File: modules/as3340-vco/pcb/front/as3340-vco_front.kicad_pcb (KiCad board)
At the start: 2 copper layers, 37.8 x 107.3 mm, 42 parts, among them J1 CV1, J2 CV2, J3 LINEAR, J4 TRIANGLE, J5 SAWTOOTH, J6 PULSE, J7 Conn_01x09, U1 TL074

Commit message: modules: as3340-vco: fix references
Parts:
- J1: value CV1 -> Thonkiconn SM
- J2: value CV2 -> Thonkiconn SM
- J3: value LINEAR -> Thonkiconn SM
- J4: value TRIANGLE -> Thonkiconn SM
- J5: value SAWTOOTH -> Thonkiconn SM
- J6: value PULSE -> Thonkiconn SM
- J7: value Conn_01x09 -> Pin Header 1x9
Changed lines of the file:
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@@
   (page A4)
   (title_block
-    (title "as3340-vco front board")
+    (title "as3340-vco front")
     (date 2021-12-14)
     (rev 1.0)
@@
     (46 B.CrtYd user)
     (47 F.CrtYd user)
-    (48 B.Fab user)
+    (48 B.Fab user hide)
     (49 F.Fab user hide)
   )
@@
       (effects (font (size 1 1) (thickness 0.15)) (justify mirror))
     )
-    (fp_text value Conn_01x09 (at 0 -22.65) (layer B.Fab)
+    (fp_text value "Pin Header 1x9" (at 0 -22.65) (layer B.Fab)
       (effects (font (size 1 1) (thickness 0.15)) (justify mirror))
     )
@@
       (effects (font (size 1 1) (thickness 0.15)))
     )
-    (fp_text value SAWTOOTH (at 0 -5) (layer F.Fab)
+    (fp_text value "Thonkiconn SM" (at 0 -5) (layer F.Fab)
       (effects (font (size 1 1) (thickness 0.15)))
     )
@@
       (effects (font (size 1 1) (thickness 0.15)))
     )
-    (fp_text value PULSE (at 0 -5) (layer F.Fab)
+    (fp_text value "Thonkiconn SM" (at 0 -5) (layer F.Fab)
       (effects (font (size 1 1) (thickness 0.15)))
     )
@@
       (effects (font (size 1 1) (thickness 0.15)))
     )
-    (fp_text value LINEAR (at 0 -5) (layer F.Fab)
+    (fp_text value "Thonkiconn SM" (at 0 -5) (layer F.Fab)
       (effects (font (size 1 1) (thickness 0.15)))
     )
@@
       (effects (font (size 1 1) (thickness 0.15)))
     )
-    (fp_text value TRIANGLE (at 0 -5) (layer F.Fab)
+    (fp_text value "Thonkiconn SM" (at 0 -5) (layer F.Fab)
       (effects (font (size 1 1) (thickness 0.15)))
     )
@@
       (effects (font (size 1 1) (thickness 0.15)))
     )
-    (fp_text value CV2 (at 0 -5) (layer F.Fab)
+    (fp_text value "Thonkiconn SM" (at 0 -5) (layer F.Fab)
       (effects (font (size 1 1) (thickness 0.15)))
     )
@@
       (effects (font (size 1 1) (thickness 0.15)))
     )
-    (fp_text value CV1 (at 0 -5) (layer F.Fab)
-      (effects (font (size 1 1) (thickness 0.15)))
-    )
+    (fp_text value "Thonkiconn SM" (at 0 -5) (layer F.Fab)
+      (effects (font (size 1 1) (thickness 0.15)))
+    )

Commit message: modules: as3340-vco: front: upgrade to kicad 6
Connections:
- J1 pad TN: (no net) -> unconnected-(J1-PadTN)
- J2 pad TN: (no net) -> unconnected-(J2-PadTN)
- J3 pad TN: (no net) -> unconnected-(J3-PadTN)
- J4 pad TN: (no net) -> unconnected-(J4-PadTN)
- J5 pad TN: (no net) -> unconnected-(J5-PadTN)
- J6 pad TN: (no net) -> unconnected-(J6-PadTN)
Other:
- net class Default removed

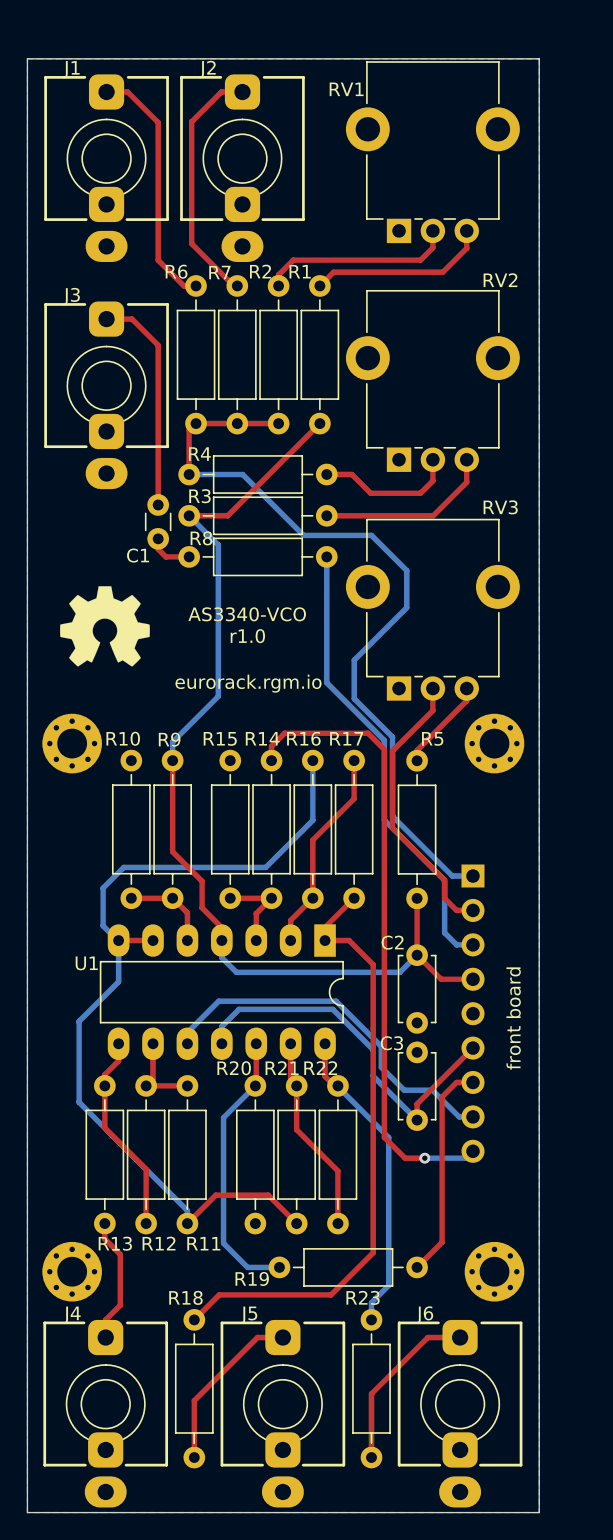
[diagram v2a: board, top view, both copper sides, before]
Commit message: modules: as3340-vco: front: revision A (redesign)
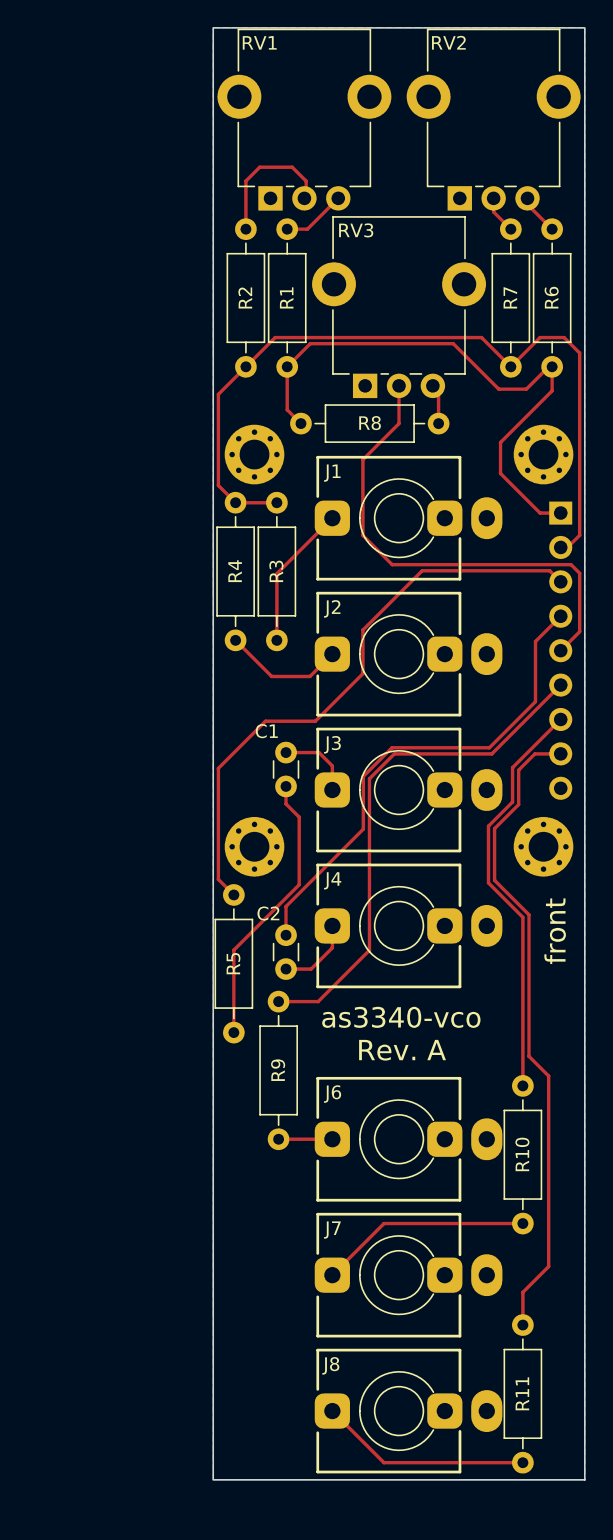
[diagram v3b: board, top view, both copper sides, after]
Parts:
- removed C3: 100n, Capacitor_THT:C_Disc_D4.7mm_W2.5mm_P5.00mm
- removed R12, R17, R22: 150k, Resistor_THT:R_Axial_DIN0207_L6.3mm_D2.5mm_P10.16mm_Horizontal
- removed R13, R18, R23: 1k, Resistor_THT:R_Axial_DIN0207_L6.3mm_D2.5mm_P10.16mm_Horizontal
- removed R14, R15, R16, R21: 100k, Resistor_THT:R_Axial_DIN0207_L6.3mm_D2.5mm_P10.16mm_Horizontal
- removed R19: 120k, Resistor_THT:R_Axial_DIN0207_L6.3mm_D2.5mm_P10.16mm_Horizontal
- removed R20: 68k, Resistor_THT:R_Axial_DIN0207_L6.3mm_D2.5mm_P10.16mm_Horizontal
- removed U1: TL074, Package_DIP:DIP-14_W7.62mm_LongPads
- added J8: Thonkiconn SM, eurorack:Jack_3.5mm_QingPu_WQP-PJ398SM_Vertical, F.Cu at (153.3, 145.2)
- added REF**: Eurorack_PCB_6HP, eurorack:Eurorack_PCB_6HP, F.Cu at (153.3, 96.6)
- C2: value 100n -> 1n; footprint Capacitor_THT:C_Disc_D4.7mm_W2.5mm_P5.00mm -> Capacitor_THT:C_Disc_D3.0mm_W1.6mm_P2.50mm
- H1, H2, H3, H4: value MountingHole -> MountingHole_Pad
- J5: value Thonkiconn SM -> Pin Header 1x9; footprint eurorack:Jack_3.5mm_QingPu_WQP-PJ398SM_Vertical -> Connector_PinHeader_2.54mm:PinHeader_1x09_P2.54mm_Vertical; moved to B.Cu
- J7: value Pin Header 1x9 -> Thonkiconn SM; footprint Connector_PinHeader_2.54mm:PinHeader_1x09_P2.54mm_Vertical -> eurorack:Jack_3.5mm_QingPu_WQP-PJ398SM_Vertical; moved to F.Cu
- R10: value 18k -> 1k
- R11: value 100k -> 1k
- R3: value 120k -> 100k
- R4: value 1.5M -> 100k
- R5: value 100k -> 1M
- R6: value 100k -> 120k
- R7: value 100k -> 1.5M
- R8: value 1M -> 100k
- R9: value 47k -> 1k
- REF**: moved to B.Cu
- moved H2 69.6 mm to (164.0, 74.5), turned to 0 degrees
- moved J5 68.9 mm to (165.2, 78.9), turned to 180 degrees
- moved J4 41.4 mm to (153.3, 109.3), turned to 90 degrees
- moved J2 38.4 mm to (153.3, 89.3), turned to 90 degrees
- moved R10 37.6 mm to (162.4, 131.3)
- moved R11 37.2 mm to (162.4, 149.0), turned to 90 degrees
- moved J3 36.8 mm to (153.3, 99.3), turned to 90 degrees
- moved H3 36.0 mm to (142.6, 103.5), turned to 0 degrees
- moved J1 34.2 mm to (153.3, 79.2), turned to 90 degrees
- moved J7 30.0 mm to (153.3, 135.1), turned to 90 degrees
- moved R9 29.0 mm to (144.4, 125.1), turned to 90 degrees
- moved R6 26.6 mm to (164.6, 68.1)
- moved H1 25.2 mm to (142.6, 74.5), turned to 0 degrees
- moved RV3 22.5 mm to (150.8, 69.5)
- moved REF** 21.8 mm to (153.2, 84.2), turned to 180 degrees
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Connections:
- C2 pad 1: +12V -> VHSI
- C2 pad 2: GND -> Net-(C2-Pad2)
- H1 pad 1: (no net) -> GND
- H2 pad 1: (no net) -> GND
- H3 pad 1: (no net) -> GND
- H4 pad 1: (no net) -> GND
- J4 pad T: Net-(J4-PadT) -> Net-(C2-Pad2)
- R10 pad 1: Net-(R10-Pad1) -> Net-(J7-PadT)
- R10 pad 2: GND -> OUT_SAWTOOTH
- R11 pad 2: VREF -> OUT_PULSE
- R3 pad 1: +12V -> VFCI
- R3 pad 2: Net-(R3-Pad2) -> Net-(J1-PadT)
- R4 pad 2: Net-(R4-Pad2) -> Net-(J2-PadT)
- R5 pad 1: +12V -> VLFI
- R5 pad 2: Net-(R5-Pad2) -> Net-(C1-Pad1)
- R6 pad 1: VFCI -> +12V
- R6 pad 2: Net-(J1-PadT) -> Net-(R6-Pad2)
- R7 pad 2: Net-(J2-PadT) -> Net-(R7-Pad2)
- R8 pad 1: VLFI -> +12V
- R8 pad 2: Net-(C1-Pad1) -> Net-(R8-Pad2)
- R9 pad 1: +12V -> Net-(J6-PadT)
- R9 pad 2: Net-(R10-Pad1) -> OUT_TRIANGLE
- RV2 pad 2: Net-(R4-Pad2) -> Net-(R7-Pad2)
- RV2 pad 3: Net-(R3-Pad2) -> Net-(R6-Pad2)
- RV3 pad 3: Net-(R5-Pad2) -> Net-(R8-Pad2)
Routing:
- net VREF: track 64.1 -> 0.00 mm
- net OUT_PULSE: track 0.00 -> 47.7 mm
- net VSO: track 46.3 -> 0.00 mm, vias 1 -> 0
- net Net-(R17-Pad1): track 44.8 -> 0.00 mm
- net OUT_TRIANGLE: track 0.00 -> 37.9 mm
- net VHSI: track 0.00 -> 36.2 mm
- net +12V: track 73.3 -> 42.1 mm
- net OUT_SAWTOOTH: track 0.00 -> 30.3 mm
- net -12V: track 27.8 -> 0.00 mm
- net VTO: track 27.3 -> 0.00 mm
- net Net-(R22-Pad1): track 23.0 -> 0.00 mm
- net Net-(R19-Pad2): track 20.6 -> 0.00 mm
- net Net-(C1-Pad1): track 3.28 -> 20.6 mm
- net VP: track 16.1 -> 0.00 mm
- net Net-(J7-PadT): track 0.00 -> 15.6 mm
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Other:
- board size 37.8 x 107.3 mm -> 27.4 x 107.2 mm
- board text added: "as3340-vco Rev. A"
- board text added: "front"
- board text removed: "AS3340-VCO r1.0"
- board text removed: "front board"
